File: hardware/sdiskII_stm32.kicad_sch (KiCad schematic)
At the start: 23 parts, among them J1 PWR, J2 APPLE_SDISKII, J3 Conn_01x06, J4 UART, J5 Conn_01x04, J6 STLINK, U2 MicroSD_SDIO, U8 DM-OLED096-636

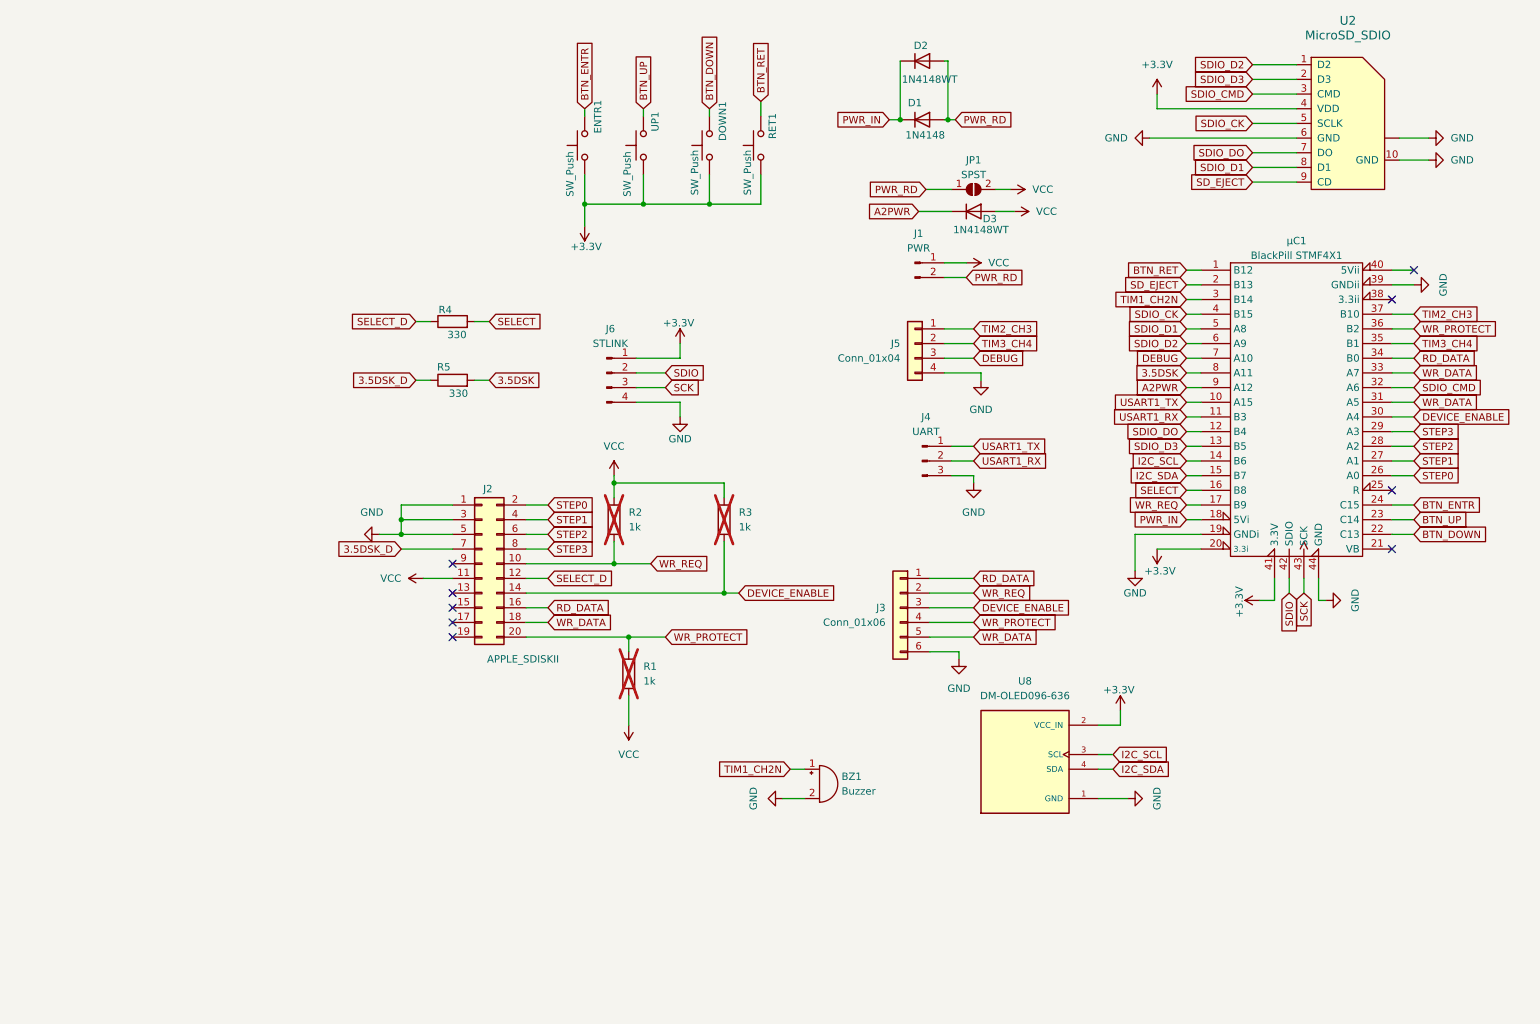
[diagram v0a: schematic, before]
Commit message: fixing Smartport on IIe II+ Rev6 Hardware
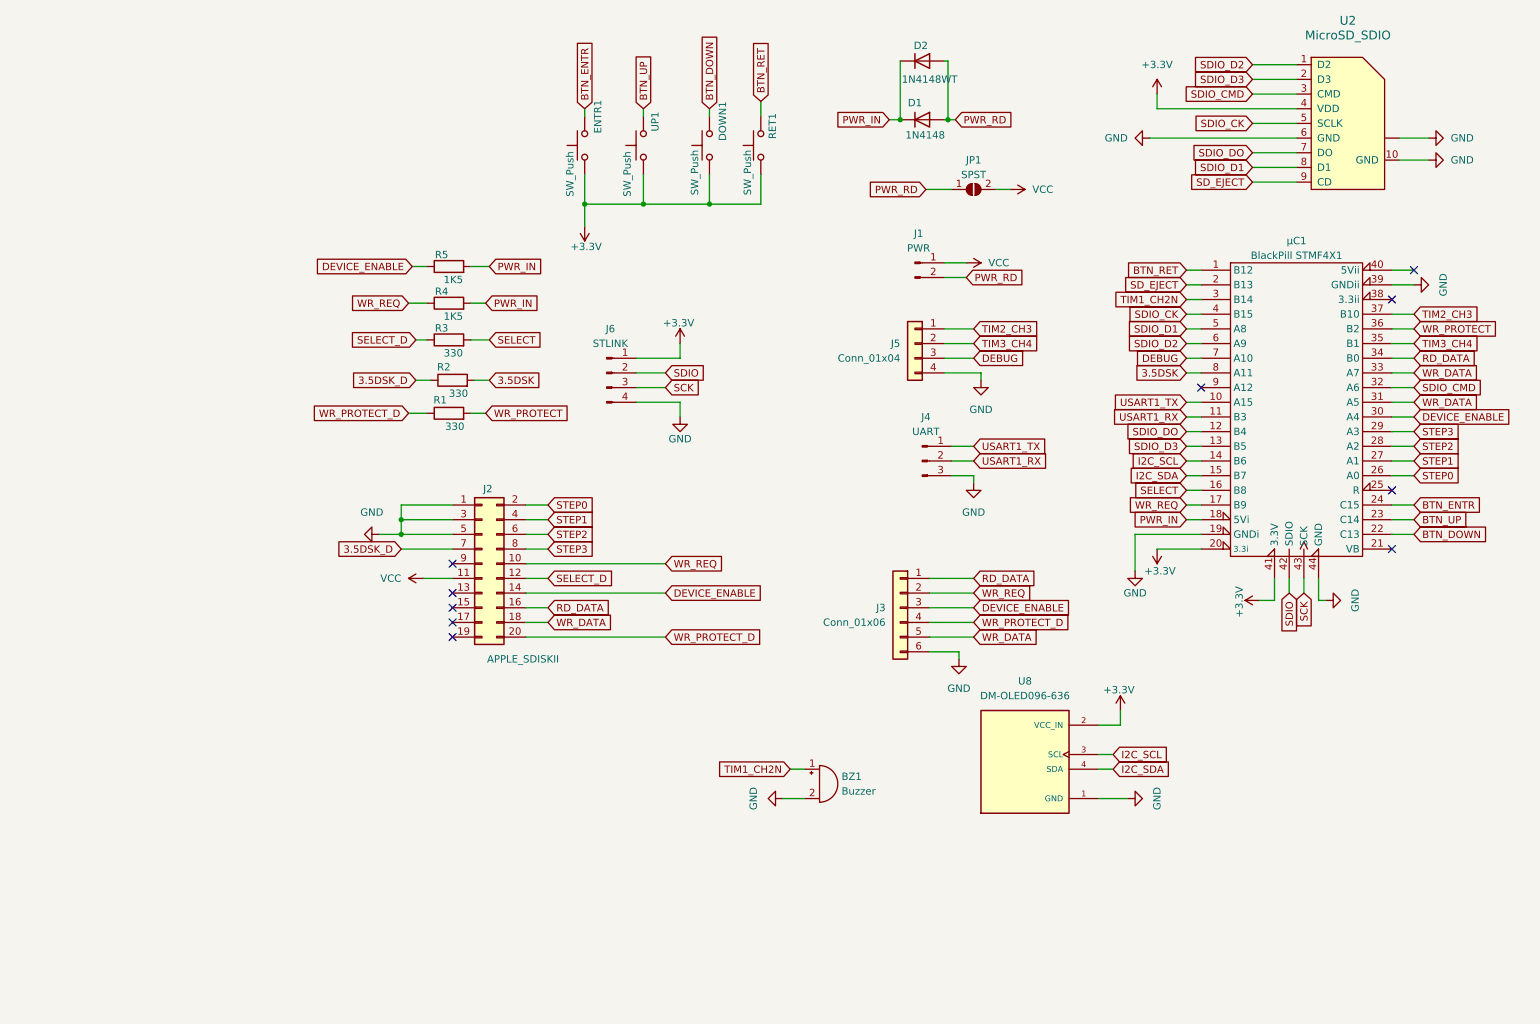
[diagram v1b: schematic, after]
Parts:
- removed D3: 1N4148WT, Diode_SMD:D_0805_2012Metric_Pad1.15x1.40mm_HandSolder, symbol Diode:1N4148WT
- removed R2, R3: 1k, Resistor_THT:R_Axial_DIN0207_L6.3mm_D2.5mm_P10.16mm_Horizontal, symbol Device:R
- added R4, R5: 1K5, Resistor_SMD:R_0805_2012Metric_Pad1.20x1.40mm_HandSolder, symbol Device:R
- R1: value 1k -> 330; footprint Resistor_THT:R_Axial_DIN0207_L6.3mm_D2.5mm_P10.16mm_Horizontal -> Resistor_SMD:R_0805_2012Metric_Pad1.20x1.40mm_HandSolder; now fitted; now in the parts list
- renumbered R5 to R2, R4 to R3
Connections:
- net DEVICE_ENABLE: now also R5.1
- net PWR_IN: now also R4.2, R5.2
- net VCC: no longer R1.2
- net WR_PROTECT: now also R1.2; no longer J2.20 (Pin_20), J3.4 (Pin_4), R1.1
- net WR_REQ: now also R4.1
- net A2PWR: no longer names the net of μC1.9 (A12)
- new net WR_PROTECT_D: J2.20 (Pin_20), J3.4 (Pin_4), R1.1
- no-connect marks 9 -> 10
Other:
- moved on the sheet: R3

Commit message: Board rev7 beta
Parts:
- added C1, C2: 10uF, Capacitor_SMD:C_0805_2012Metric_Pad1.18x1.45mm_HandSolder, symbol Device:C
- added Fu2: Polyfuse 500mA, Fuse:Fuse_0805_2012Metric_Pad1.15x1.40mm_HandSolder, symbol Device:Polyfuse
- added J7: PWR, Connector_PinHeader_2.54mm:PinHeader_1x02_P2.54mm_Vertical, symbol Connector:Conn_01x02_Pin
- added JP2: SPST, Jumper:SolderJumper-2_P1.3mm_Open_RoundedPad1.0x1.5mm, symbol Jumper:SolderJumper_2_Open
- added U1: LM1117MP-3.3, Package_TO_SOT_SMD:SOT-223-3_TabPin2, symbol Regulator_Linear:LM1117MP-3.3
- R1, R2, R3: value 330 -> 330R
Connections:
- net +3.3V: now also J7.1 (Pin_1), JP2.2 (B)
- net GND: now also C1.2, C2.2, U1.1 (GND)
- net PWR_RD: now also D1.1 (K), D2.1 (K), R4.2, R5.2, C2.1, U1.3 (VI); no longer D1.2 (A), D2.2 (A)
- net VCC: now also Fu2.2; no longer J1.1 (Pin_1), JP1.2 (B)
- removed net PWR_IN: D1.1 (K), D2.1 (K), R4.2, R5.2, μC1.18 (5Vi)
- new net: D1.2 (A), D2.2 (A), Fu2.1
- new net: C1.1, J7.2 (Pin_2), JP2.1 (A), U1.2 (VO)
- new net PWR_5VIN: J1.1 (Pin_1), JP1.2 (B), μC1.18 (5Vi)
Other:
- company: (none) -> Vincent BESSON
- title: APPLE II DISK EM STM32F411 -> SMARTDISK II  STM32F411
- moved on the sheet: JP1, R2

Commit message: v0.80.17 Alpha
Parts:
- added JP3: BYP, Jumper:SolderJumper-2_P1.3mm_Open_RoundedPad1.0x1.5mm, symbol Jumper:SolderJumper_2_Open
- J3: value Conn_01x06 -> A2PIN
- J5: value Conn_01x04 -> DEBUG
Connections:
- net VCC: now also JP3.2 (B)
- net at D1.2 (A), D2.2 (A), Fu2.1: now also JP3.1 (A)
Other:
- moved on the sheet: D1, D2, Fu2, J1, JP1

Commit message: Board Rev7 beta 2 # Add bypass pads
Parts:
- added BPR1, BPR2, BPR3: BYP, Jumper:SolderJumper-2_P1.3mm_Open_RoundedPad1.0x1.5mm, symbol Jumper:SolderJumper_2_Open
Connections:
- net 3.5DSK: now also BPR2.2 (B)
- net 3.5DSK_D: now also BPR2.1 (A)
- net SELECT: now also BPR3.2 (B)
- net SELECT_D: now also BPR3.1 (A)
- net WR_PROTECT: now also BPR1.2 (B)
- net WR_PROTECT_D: now also BPR1.1 (A)
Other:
- moved on the sheet: R1, R2, R3, R4, R5

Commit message: 0.80.17 beta 4
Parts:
- renumbered JP3 to BPF, Fu2 to Fu1
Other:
- moved on the sheet: R4, R5
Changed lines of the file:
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@@
 	(wire
 		(pts
-			(xy 96.52 55.88) (xy 99.695 55.88)
+			(xy 45.72 52.705) (xy 48.895 52.705)
 		)
 		(stroke
@@
 	(wire
 		(pts
-			(xy 96.52 49.53) (xy 99.695 49.53)
+			(xy 45.72 46.355) (xy 48.26 46.355)
 		)
 		(stroke
@@
 	(wire
 		(pts
-			(xy 86.36 49.53) (xy 88.9 49.53)
+			(xy 36.195 46.355) (xy 38.1 46.355)
 		)
 		(stroke
@@
 	(wire
 		(pts
-			(xy 85.725 55.88) (xy 88.9 55.88)
+			(xy 36.195 52.705) (xy 38.1 52.705)
 		)
 		(stroke
@@
 	(global_label "DEVICE_ENABLE"
 		(shape input)
-		(at 86.36 49.53 180)
+		(at 36.195 46.355 180)
 		(fields_autoplaced yes)
 		(effects
@@
 		)
 		(property "Intersheetrefs" "${INTERSHEET_REFS}"
-			(at 68.8606 49.53 0)
+			(at 18.6956 46.355 0)
 			(effects
 				(font
@@
 	(global_label "WR_REQ"
 		(shape input)
-		(at 85.725 55.88 180)
+		(at 36.195 52.705 180)
 		(fields_autoplaced yes)
 		(effects
@@
 		)
 		(property "Intersheetrefs" "${INTERSHEET_REFS}"
-			(at 75.3013 55.88 0)
+			(at 25.7713 52.705 0)
 			(effects
 				(font
@@
 	(global_label "PWR_RD"
 		(shape input)
-		(at 99.695 49.53 0)
+		(at 48.26 46.355 0)
 		(fields_autoplaced yes)
 		(effects
@@
 		)
 		(property "Intersheetrefs" "${INTERSHEET_REFS}"
-			(at 110.1792 49.53 0)
+			(at 58.7442 46.355 0)
 			(effects
 				(font
@@
 	(global_label "PWR_RD"
 		(shape input)
-		(at 99.695 55.88 0)
+		(at 48.895 52.705 0)
 		(fields_autoplaced yes)
 		(effects
@@
 		)
 		(property "Intersheetrefs" "${INTERSHEET_REFS}"
-			(at 110.1792 55.88 0)
+			(at 59.3792 52.705 0)
 			(effects
 				(font
@@
 		(on_board yes)
 		(dnp no)
-		(fields_autoplaced yes)
 		(property "Reference" "BPR3"
-			(at 42.545 55.245 0)
+			(at 42.672 58.928 0)
 			(effects
 				(font
@@
 		)
 		(property "Value" "BYP"
-			(at 42.545 57.785 0)
+			(at 42.672 64.008 0)
 			(effects
 				(font
@@
 		(on_board yes)
 		(dnp no)
-		(property "Reference" "Fu2"
+		(property "Reference" "Fu1"
 			(at 56.515 155.575 90)
 			(effects
@@
 			(project "sdiskII_stm32"
 				(path "/a83c7550-2269-4fd8-90ce-2da165082457"
-					(reference "Fu2")
+					(reference "Fu1")
 					(unit 1)
 				)
@@
 		(dnp no)
 		(fields_autoplaced yes)
-		(property "Reference" "JP3"
+		(property "Reference" "BPF"
 			(at 52.07 140.97 0)
 			(effects
@@
 			(project "sdiskII_stm32"
 				(path "/a83c7550-2269-4fd8-90ce-2da165082457"
-					(reference "JP3")
+					(reference "BPF")
 					(unit 1)
 				)
@@
 	(symbol
 		(lib_id "Device:R")
-		(at 92.71 55.88 90)
+		(at 41.91 52.705 90)
 		(unit 1)
 		(exclude_from_sim no)
@@
 		(dnp no)
 		(property "Reference" "R4"
-			(at 92.837 56.007 90)
+			(at 42.037 52.832 90)
 			(effects
 				(font
@@
 		)
 		(property "Value" "1K5"
-			(at 93.599 58.039 90)
+			(at 42.799 54.864 90)
 			(effects
 				(font
@@
 		)
 		(property "Footprint" "Resistor_SMD:R_0805_2012Metric_Pad1.20x1.40mm_HandSolder"
-			(at 92.71 57.658 90)
+			(at 41.91 54.483 90)
 			(effects
 				(font
@@
 		)
 		(property "Datasheet" "~"
-			(at 92.71 55.88 0)
+			(at 41.91 52.705 0)
 			(effects
 				(font
@@
 		)
 		(property "Description" "Resistor"
-			(at 92.71 55.88 0)
+			(at 41.91 52.705 0)
 			(effects
 				(font
@@
 	(symbol
 		(lib_id "Device:R")
-		(at 92.71 49.53 90)
+		(at 41.91 46.355 90)
 		(unit 1)
 		(exclude_from_sim no)
@@
 		(dnp no)
 		(property "Reference" "R5"
-			(at 92.837 49.657 90)
+			(at 42.037 46.482 90)
 			(effects
 				(font
@@
 		)
 		(property "Value" "1K5"
-			(at 93.599 51.689 90)
+			(at 42.799 48.514 90)
 			(effects
 				(font
@@
 		)
 		(property "Footprint" "Resistor_SMD:R_0805_2012Metric_Pad1.20x1.40mm_HandSolder"
-			(at 92.71 51.308 90)
+			(at 41.91 48.133 90)
 			(effects
 				(font
@@
 		)
 		(property "Datasheet" "~"
-			(at 92.71 49.53 0)
+			(at 41.91 46.355 0)
 			(effects
 				(font
@@
 		)
 		(property "Description" "Resistor"
-			(at 92.71 49.53 0)
+			(at 41.91 46.355 0)
 			(effects
 				(font

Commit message: v0.80.20.4
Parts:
- D2: footprint Diode_SMD:D_0805_2012Metric_Pad1.15x1.40mm_HandSolder -> Diode_SMD:D_SOD-123
- renumbered BPF to BPF1
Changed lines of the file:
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@@
 			)
 		)
-		(property "Footprint" "Diode_SMD:D_0805_2012Metric_Pad1.15x1.40mm_HandSolder"
+		(property "Footprint" "Diode_SMD:D_SOD-123"
 			(at 36.83 151.13 0)
 			(effects
@@
 		(dnp no)
 		(fields_autoplaced yes)
-		(property "Reference" "BPF"
+		(property "Reference" "BPF1"
 			(at 52.07 140.97 0)
 			(effects
@@
 			(project "sdiskII_stm32"
 				(path "/a83c7550-2269-4fd8-90ce-2da165082457"
-					(reference "BPF")
-					(unit 1)
-				)
+					(reference "BPF1")
+					(unit 1)
+				)

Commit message: v0.80.27 #1
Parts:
- D2: footprint Diode_SMD:D_SOD-123 -> Diode_SMD:D_SMA_Handsoldering
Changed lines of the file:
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@@
 			)
 		)
-		(property "Footprint" "Diode_SMD:D_SOD-123"
+		(property "Footprint" "Diode_SMD:D_SMA_Handsoldering"
 			(at 36.83 151.13 0)
 			(effects

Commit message: doc
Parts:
- BZ1: Cost (none) -> $0.94; Mandatory (none) -> NO; Supply (none) -> LCSC C252917
- C1, C2: Cost (none) -> $0.01; Mandatory (none) -> NO; Supply (none) -> LCSC C15850
- D1: Cost (none) -> $0.014; Mandatory (none) -> YES or D2; Supply (none) -> LCSC C84410
- D2: value 1N4148WT -> SS16; Cost (none) -> $0.59; Mandatory (none) -> YES or D1; Supply (none) -> LCSC C908233
- DOWN1, ENTR1, RET1, UP1: Cost (none) -> $0.016; Mandatory (none) -> YES; Supply (none) -> LCSC C393938
- Fu1: Cost (none) -> $0.45; Mandatory (none) -> NO; Supply (none) -> LCSC C66452
- J2: Cost (none) -> $0.26; Mandatory (none) -> YES; Supply (none) -> LCSC C115249
- R1, R2, R3: Cost (none) -> $0.0019; Mandatory (none) -> NO; Supply (none) -> LCSC C17630
- R4, R5: Cost (none) -> $0.0021; Mandatory (none) -> NO; Supply (none) -> LCSC C114555
- U1: Cost (none) -> $0.91; Mandatory (none) -> NO; Supply (none) -> LCSC C9662
- U2: Cost (none) -> $0.08; Mandatory (none) -> YES; Supply (none) -> Mouser 640-MEM20750014001A / LCSC C381084
- U8: Cost (none) -> $2; Description_1 0.96” 128 X 64 MONOCHROME GRAPHIC OLED DISPLAY MODULE - I2C -> 0.96 128x64 SSD1315 I2C LCD, OLED, Graphic RoHS; Mandatory (none) -> YES; Supply (none) -> LCSC C5248080
- μC1: value BlackPill STMF4X1 -> STM32F411 (BlackPill) 25Mhz; Cost (none) -> $2.99; Supply (none) -> WeAct Studio 3.0 STM32F411CEU6
